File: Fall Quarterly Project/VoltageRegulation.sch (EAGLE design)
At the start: 24 parts, among them IC3 L272M

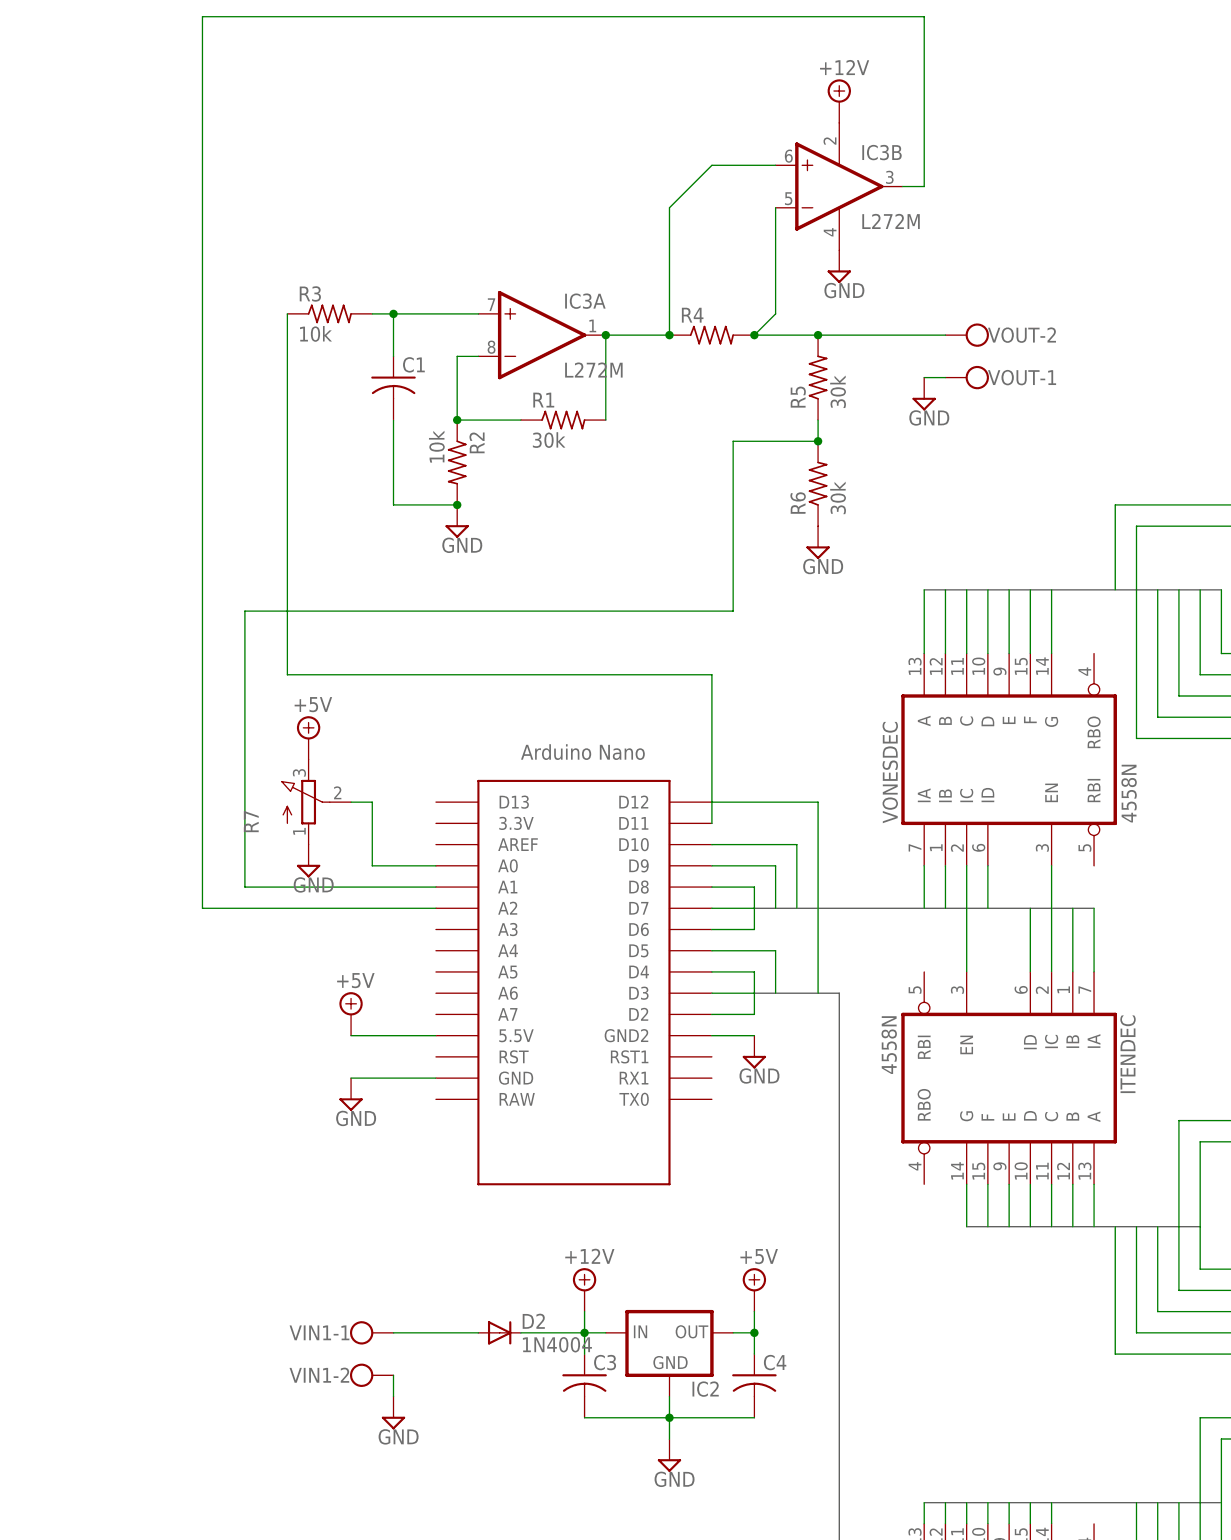
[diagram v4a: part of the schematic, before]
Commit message: Update 1.6
Fixed current sense circuit, just need to update the board layout now
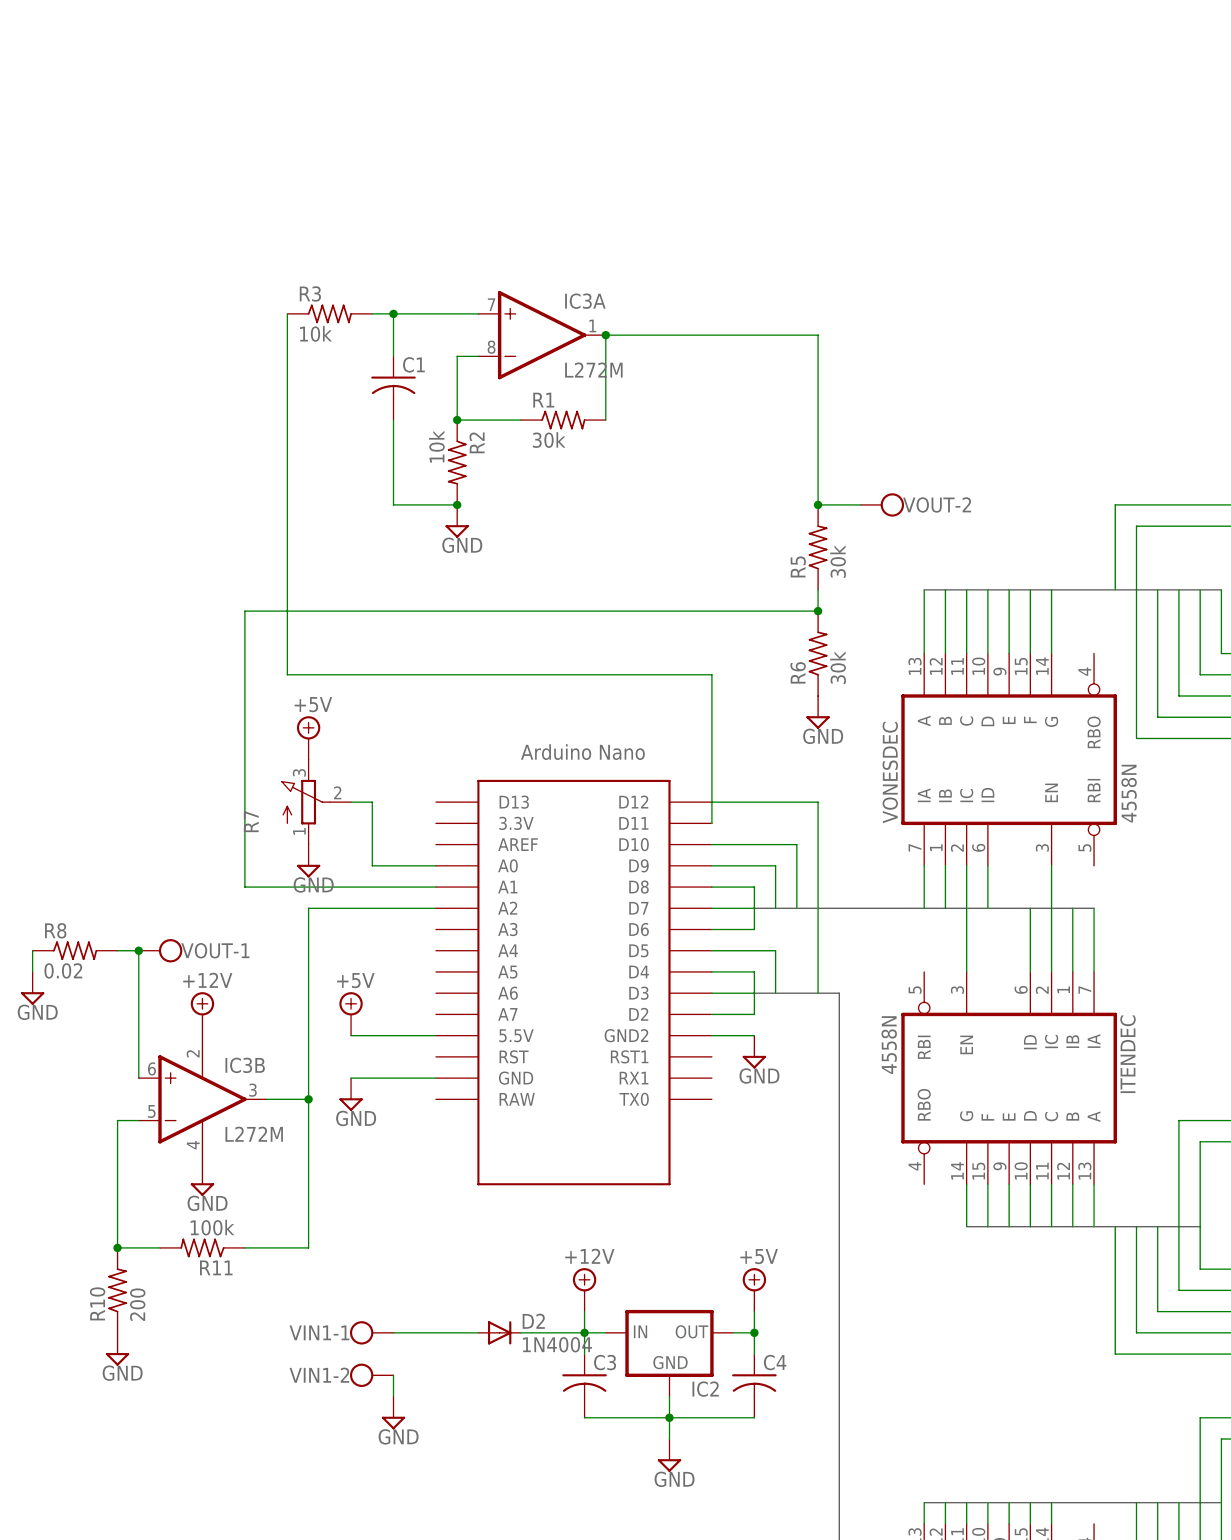
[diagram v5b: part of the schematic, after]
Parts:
- removed R4: (no value), rcl:R-US_0411/12
- added R10: 200, rcl:R-US_0207/7
- added R11: 100k, rcl:R-US_0207/7
- added R8: 0.02, rcl:R-US_0411/12
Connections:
- new net N$13: IC3B.-IN, R10.2, R11.2
- net GND: now also R10.1, R8.1; no longer VOUT-1.KL
- net N$10: now also R11.1
- net N$2: now also R8.2, VOUT-1.KL; no longer IC3A.OUT, R1.2, R4.1
- net N$6: now also IC3A.OUT, R1.2; no longer IC3B.-IN, R4.2
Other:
- moved on the sheet: IC3B, R5, R6, VOUT-1, VOUT-2
